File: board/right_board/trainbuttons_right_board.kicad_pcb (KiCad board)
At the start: 4 copper layers, 88 x 95 mm, 16 parts, among them J301 HDMI_A, SW301 SW_Push, SW302 SW_Push, SW303 SW_Push, SW304 SW_Push, SW305 SW_Push, SW306 SW_Push, SW307 SW_Push, SW308 SW_Push

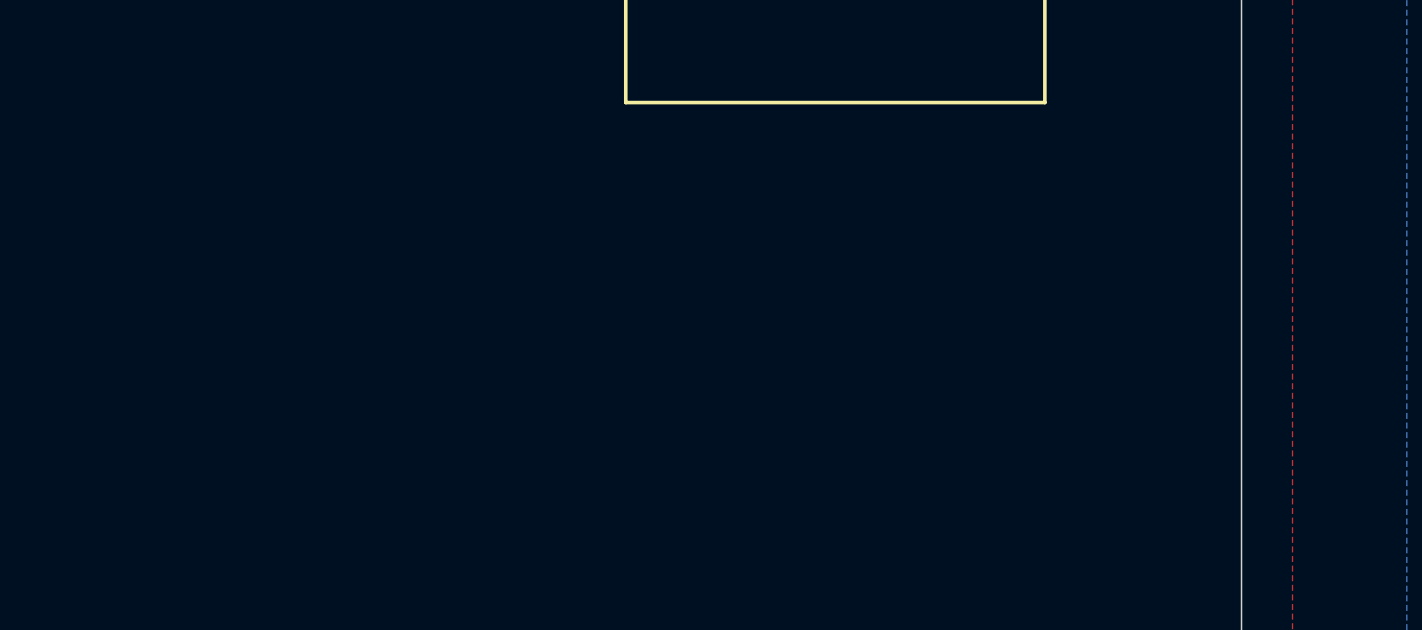
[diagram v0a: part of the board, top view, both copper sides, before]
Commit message: right: add revision text
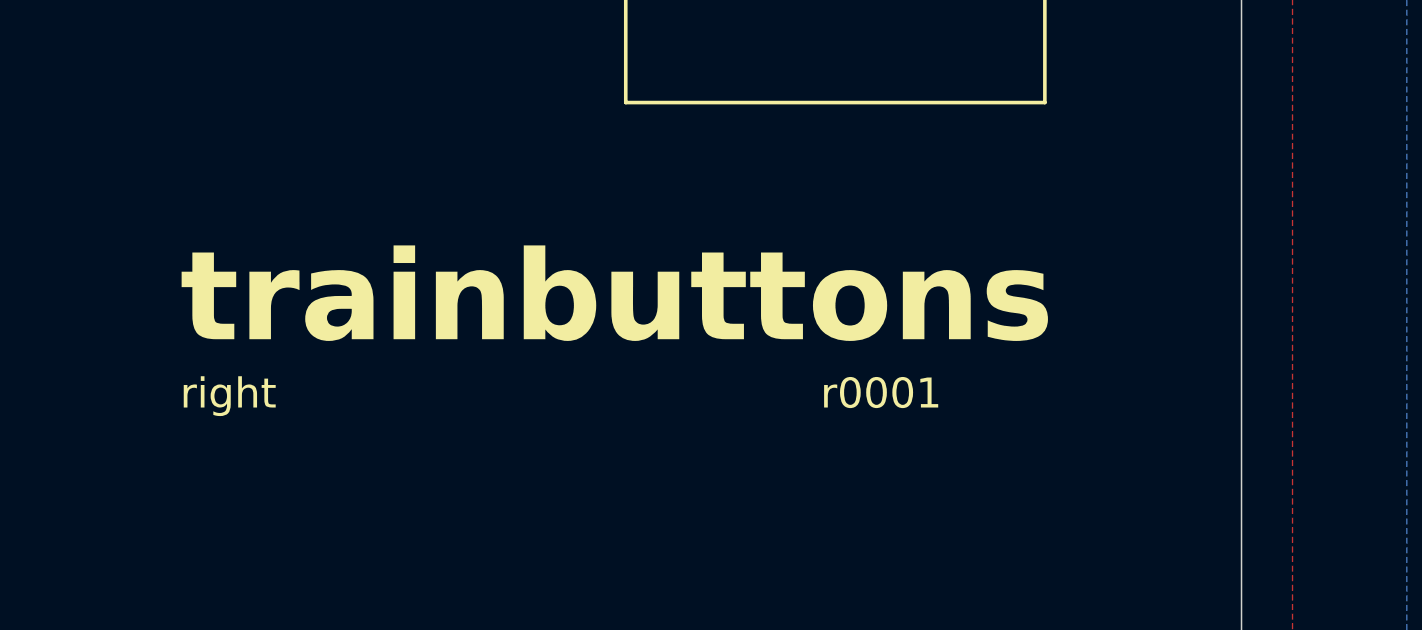
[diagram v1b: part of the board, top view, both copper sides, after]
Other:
- board text added: "r0001"
- board text added: "right"
- board text added: "trainbuttons"
